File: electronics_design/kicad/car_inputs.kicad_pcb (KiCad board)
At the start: 2 copper layers, 66.8 x 88.1 mm, 23 parts, among them J1 Conn_01x05_PinConn_Header_JST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, J2 Conn_Header_JST_PH_1x04_P2mm_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, J3 Conn_Header_JST_PH_1x04_P2mm_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, J4 Conn_Header_JST_PH_1x04_P2mm_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, J5 Conn_Header_JST_PH_1x03_P2mm_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, J6 Conn_Header_JST_PH_1x03_P2mm_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, M1 Module_XIAO-RP2040

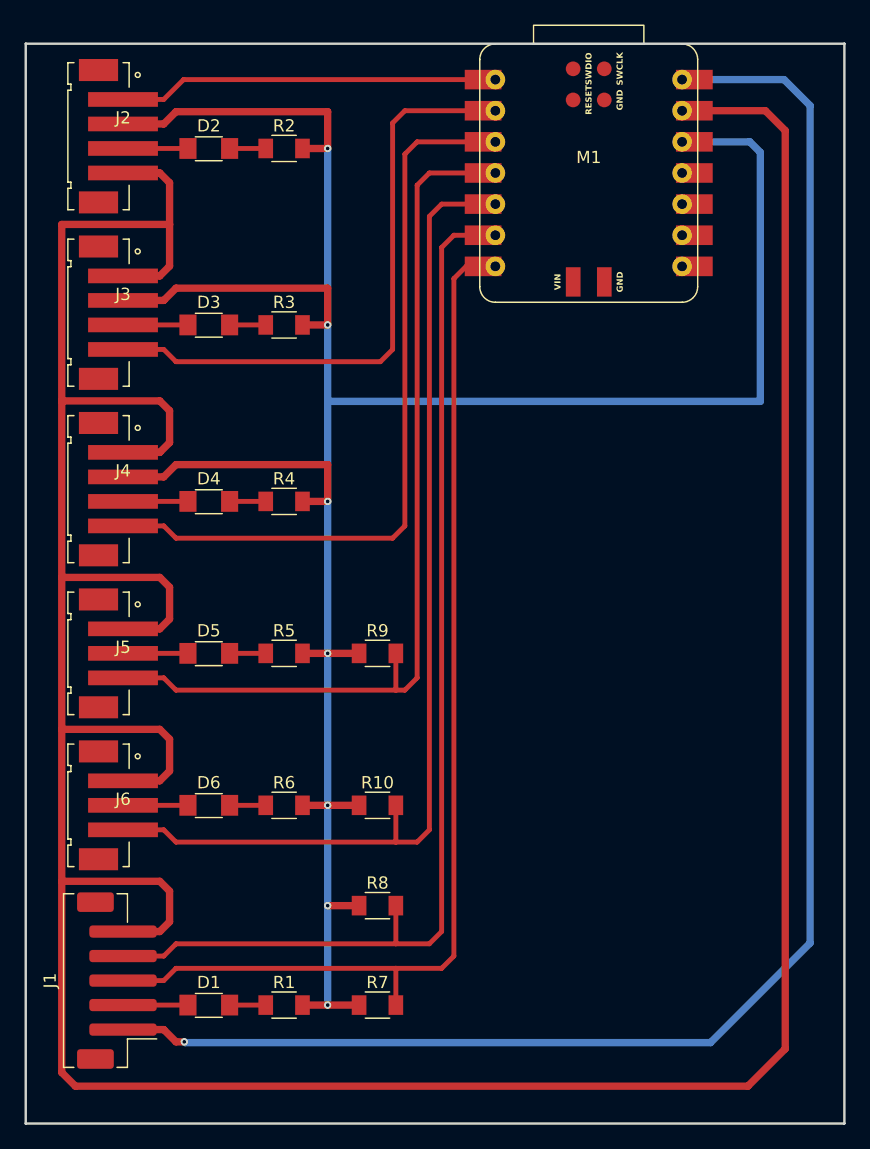
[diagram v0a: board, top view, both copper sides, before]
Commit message: Replace 5V encoder power with 3V3
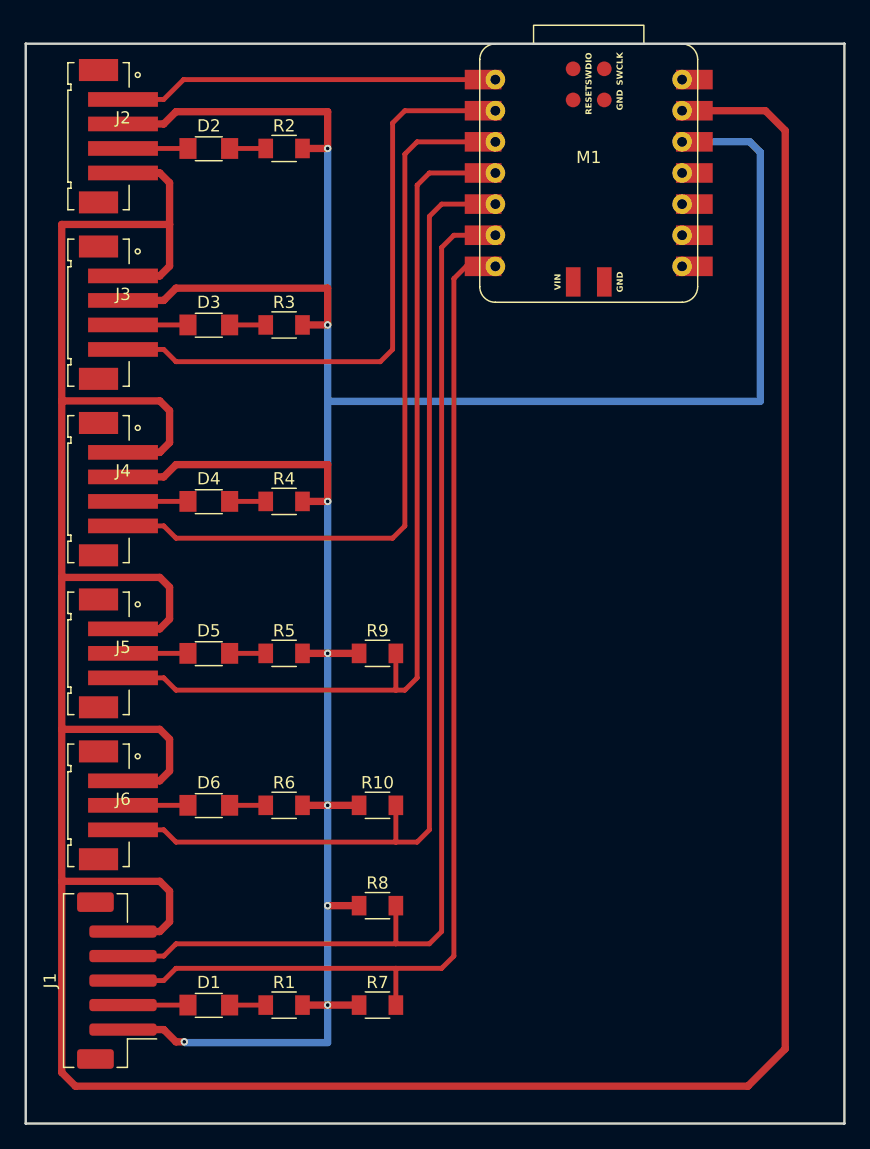
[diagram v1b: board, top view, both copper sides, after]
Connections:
- J1 pad 1: +5V -> +3V3
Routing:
- net +5V: track 139.5 -> 0.00 mm, vias 1 -> 0
- net +3V3: track 215.2 -> 235.4 mm, vias 7 -> 8
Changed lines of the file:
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@@
 			(layers "F.Cu" "F.Mask" "F.Paste")
 			(roundrect_rratio 0.25)
-			(net "+5V")
+			(net "+3V3")
 			(pinfunction "Pin_1_1")
 			(pintype "passive")
@@
 		(width 0.6)
 		(layer "F.Cu")
-		(net "+5V")
+		(net "+3V3")
 	)
 	(segment
@@
 		(width 0.6)
 		(layer "F.Cu")
-		(net "+5V")
+		(net "+3V3")
 	)
 	(segment
@@
 		(width 0.6)
 		(layer "F.Cu")
-		(net "+5V")
+		(net "+3V3")
 	)
 	(via
@@
 		(drill 0.3)
 		(layers "F.Cu" "B.Cu")
-		(net "+5V")
-	)
-	(segment
-		(start 101.346 101.6)
-		(end 101.346 33.274)
-		(width 0.6)
-		(layer "B.Cu")
-		(net "+5V")
+		(net "+3V3")
 	)
 	(segment
 		(start 50.338 109.728)
-		(end 93.218 109.728)
+		(end 61.976 109.728)
 		(width 0.6)
 		(layer "B.Cu")
-		(net "+5V")
+		(net "+3V3")
 	)
 	(segment
-		(start 99.218 31.146)
-		(end 90.896 31.146)
+		(start 61.976 106.666)
+		(end 61.976 109.728)
 		(width 0.6)
 		(layer "B.Cu")
-		(net "+5V")
+		(net "+3V3")
 	)
 	(segment
@@
 		(width 0.6)
 		(layer "B.Cu")
-		(net "+5V")
-	)
-	(segment
-		(start 93.218 109.728)
-		(end 101.346 101.6)
-		(width 0.6)
-		(layer "B.Cu")
-		(net "+5V")
-	)
-	(segment
-		(start 101.346 33.274)
-		(end 99.218 31.146)
-		(width 0.6)
-		(layer "B.Cu")
-		(net "+5V")
+		(net "+3V3")
 	)
 	(segment
